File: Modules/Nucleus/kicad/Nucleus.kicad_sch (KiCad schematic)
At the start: 49 parts, among them U1 LM358, U2 LM358, U3 LM324, U4 74HC04, U5 78L05

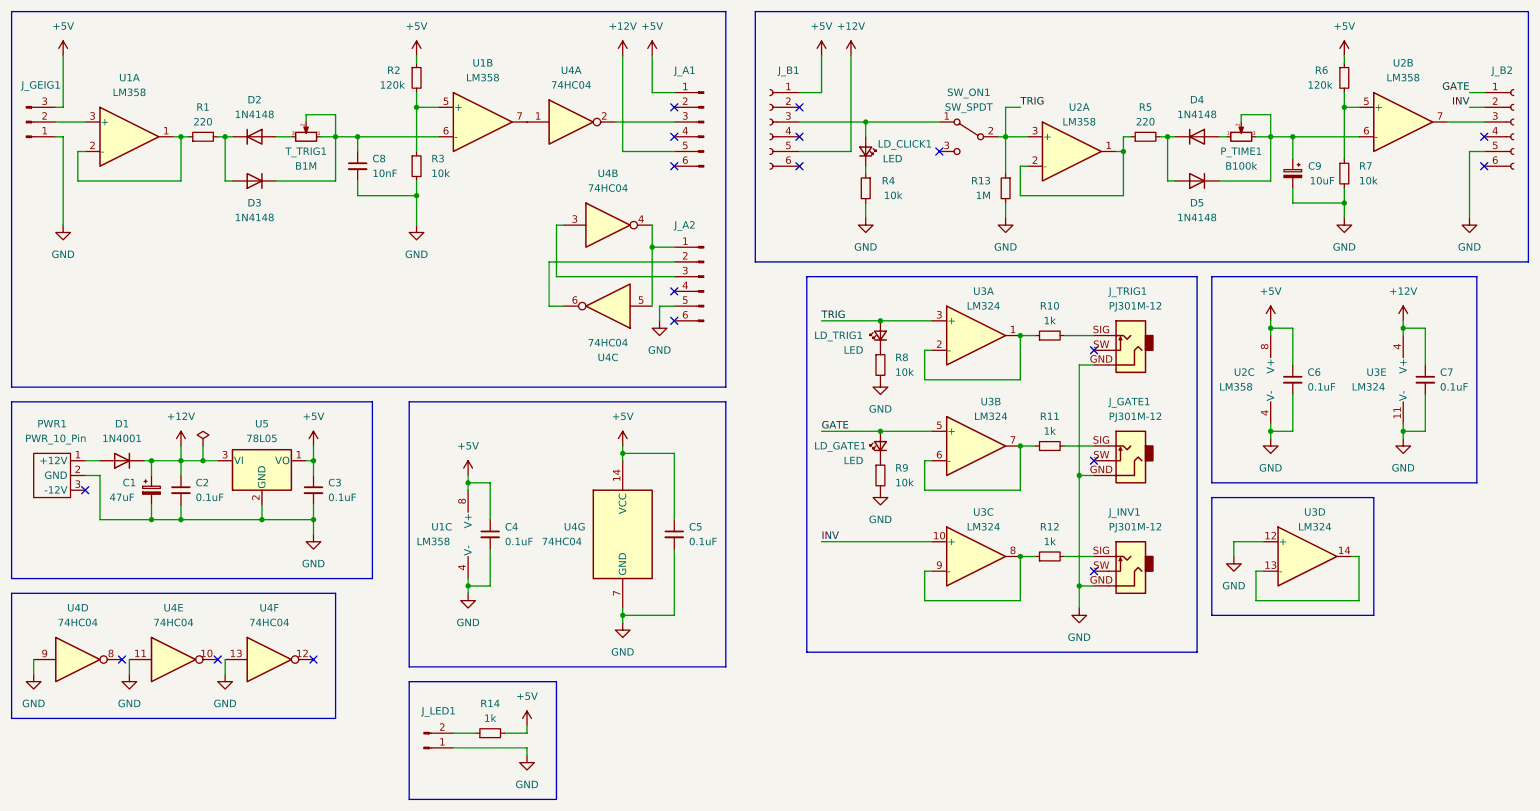
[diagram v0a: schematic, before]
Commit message: Upgrade Nucleus to 1.2, fix triggers not working.
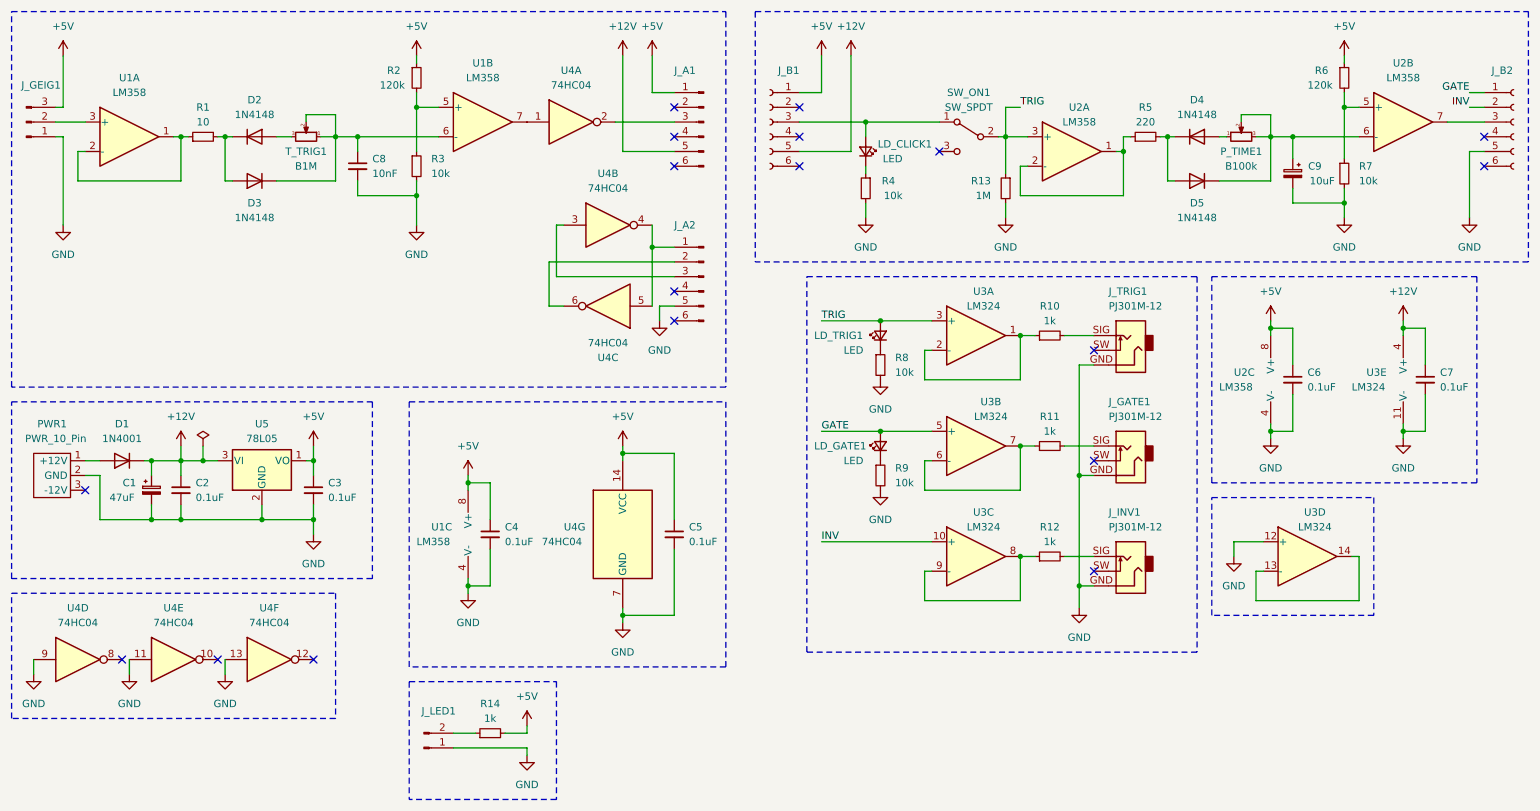
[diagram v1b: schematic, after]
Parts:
- LD_CLICK1, LD_GATE1, LD_TRIG1: Spice_Lib_File /home/ebu/Documents/KiCad/KiCad-Spice-Library/Models/Diode/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 -> (none); Spice_Model LED_GENERAL -> (none); Spice_Netlist_Enabled Y -> (none); Spice_Primitive D -> (none)
- R1: value 220 -> 10
- U3: Spice_Lib_File /home/ebu/Documents/KiCad/KiCad-Spice-Library/Models/uncate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 -> (none); Spice_Model LM324 -> (none); Spice_Netlist_Enabled Y -> (none); Spice_Primitive X -> (none)
